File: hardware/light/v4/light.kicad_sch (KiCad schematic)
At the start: 18 parts, among them J1 PH2-16-UA, J2 Conn_01x09, J3 Conn_01x09, J4 B3B-XH-A, Q1 DMG2301L, Q2 MMBT3904, U1 LP2985-50DBVR, U2 SN74LVC1G17DBVR

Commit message: Wordsmithing and link to firmware repo.
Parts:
- added D1: 5.1V, Diode_SMD:D_SOD-123, symbol Device:D_Zener
- added R5: 100K, Resistor_SMD:R_0603_1608Metric, symbol Device:R
- Q1: value DMG2301L -> SI2301CDS; Alternative (none) -> DMG2301L; LCSC C102619 -> C10487; LCSC_Alternative (none) -> C102619
- renumbered R5 to R6, R6 to R7
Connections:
- net +12V: now also D1.1 (K)
- net GND: now also R5.1
- net LOAD: now also R5.2
- net at Q1.1 (G), R1.2, R2.2: now also D1.2 (A)
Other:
- note added: "Suitable for PWM switching LEDs at 1 KHz"
- note removed: "Suitable for PWM switching at low frequencies (< 1 KHz) DMG2301L parameters - Vgss max = -8 V - Vdss max = -20 V - Id max = -3 A - Rds(on) max = 120 mOhm"
- moved on the sheet: C1, C2, C3, J1, J2, J3, J4, JP1, Q1, R3, R4, R6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

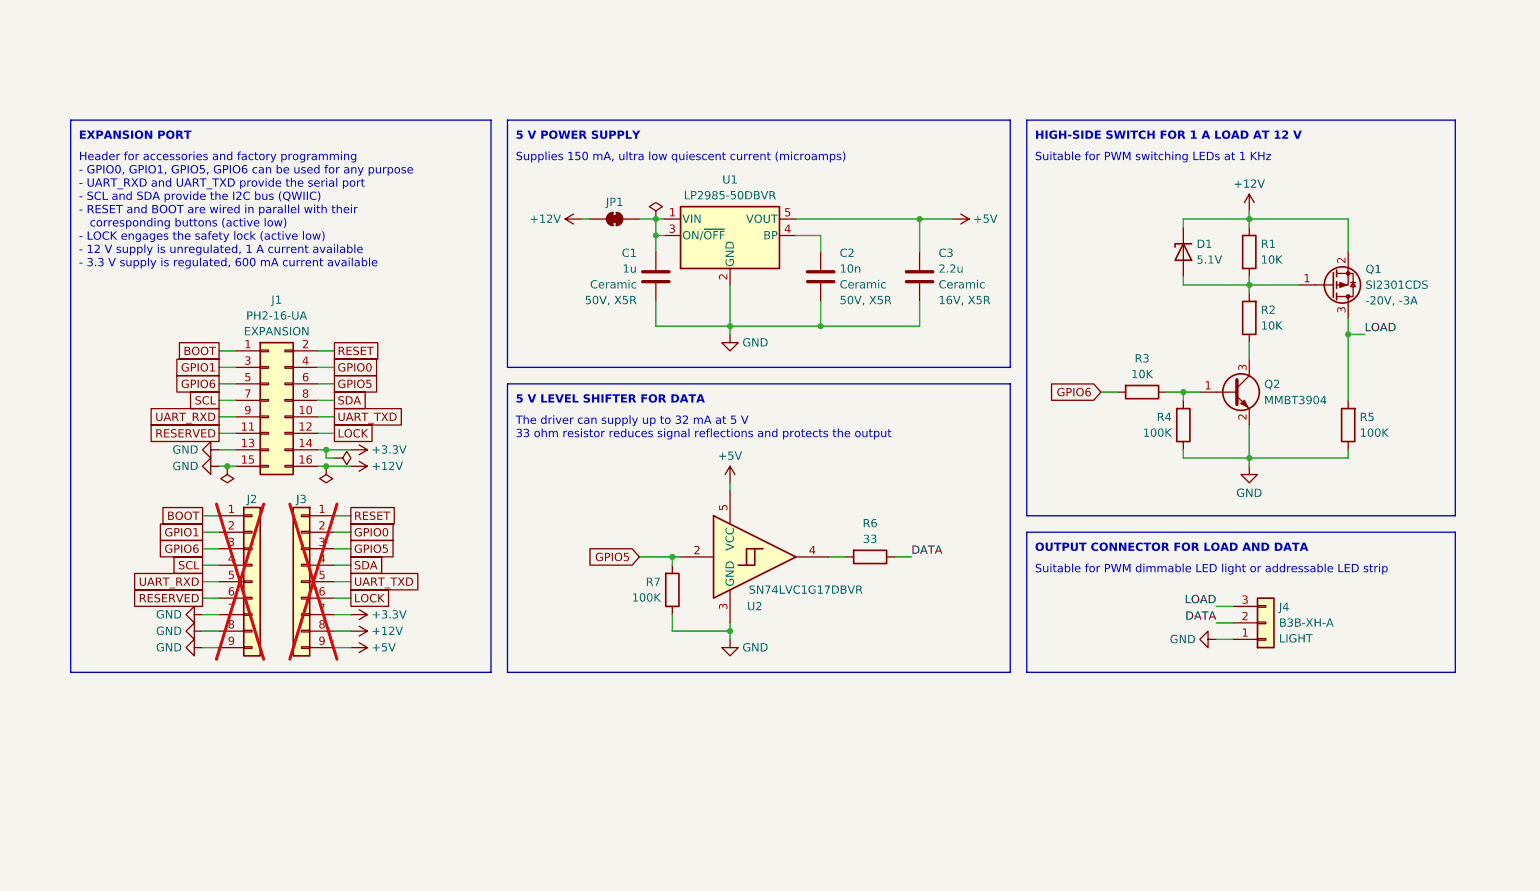
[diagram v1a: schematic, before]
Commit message: First draft of Minuet light accessory v4.
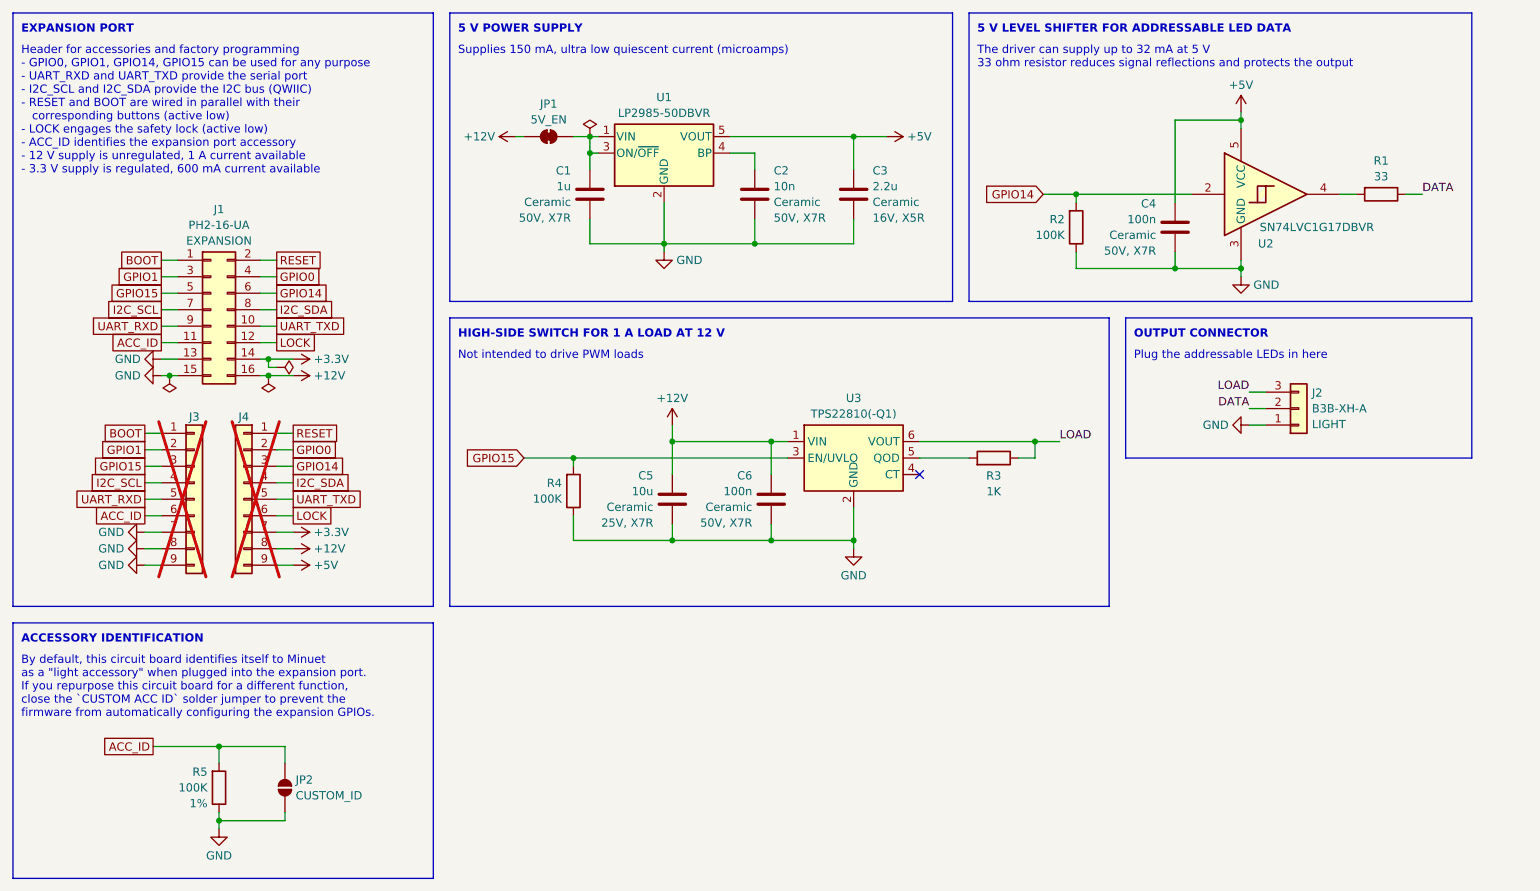
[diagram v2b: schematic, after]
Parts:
- removed D1: 5.1V, Diode_SMD:D_SOD-123, symbol Device:D_Zener
- removed Q1: SI2301CDS, Package_TO_SOT_SMD:SOT-23, symbol Transistor_FET:Q_PMOS_GSD
- removed Q2: MMBT3904, Package_TO_SOT_SMD:SOT-23, symbol Transistor_BJT:MMBT3904
- removed R1, R2: 10K, Resistor_SMD:R_0603_1608Metric, symbol Device:R
- added C4, C6: 100n, Capacitor_SMD:C_0603_1608Metric, symbol Device:C
- added C5: 10u, Capacitor_SMD:C_1210_3225Metric, symbol Device:C
- added JP2: SolderJumper_2_Open, Jumper:SolderJumper-2_P1.3mm_Open_RoundedPad1.0x1.5mm, symbol Jumper:SolderJumper_2_Open
- added U3: TPS22810(-Q1), Package_TO_SOT_SMD:SOT-23-6, symbol Power_Management:TPS22810DBV
- C1: footprint Capacitor_SMD:C_0603_1608Metric -> Capacitor_SMD:C_0805_2012Metric; LCSC C15849 -> C28323; Rating 50V, X5R -> 50V, X7R
- C2: Rating 50V, X5R -> 50V, X7R
- JP1: Label (none) -> 5V_EN
- R1: renamed from R6; Rating (none) -> 1%
- R2: renamed from R7; Rating (none) -> 1%
- R3: value 10K -> 1K; LCSC C25804 -> C21190; Rating (none) -> 1%
- R4, R5: Rating (none) -> 1%
- renumbered J4 to J2, J2 to J3, J3 to J4
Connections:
- net +12V: now also C5.1, C6.1, U3.1 (VIN)
- net +5V: now also C4.1
- net GND: now also C4.2, C5.2, C6.2, JP2.2 (B), U3.2 (GND)
- net LOAD: now also R3.1, U3.6 (VOUT); no longer R5.2
- net GPIO15: now reaches R4.2
- net GPIO15: now also J1.5 (Pin_5), J3.3 (Pin_3), U3.3 (EN/UVLO); no longer R3.1
- net GPIO5 renamed GPIO14
- removed net GPIO6: J1.5 (Pin_5), J3.3 (Pin_3), R3.2
- net RESERVED renamed ACC_ID
- net ACC_ID: now also R5.2, JP2.1 (A)
- net SCL renamed I2C_SCL
- net SDA renamed I2C_SDA
- new net: R3.2, U3.5 (QOD)
- no-connect marks 0 -> 1
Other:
- note added: "5 V LEVEL SHIFTER FOR ADDRESSABLE LED DATA"
- note added: "ACCESSORY IDENTIFICATION"
- note added: "By default, this circuit board identifies itself to Minuet as a "light accessory" when plugged into the expansion port. If you repurpose this circuit board for a different function, close the `CUSTOM ACC ID` solder jumper to prevent the firmware from automatically configuring the expansion GPIOs."
- note added: "Header for accessories and factory programming - GPIO0, GPIO1, GPIO14, GPIO15 can be used for any purpose - UART_RXD and UART_TXD provide the serial port - I2C_SCL and I2C_SDA provide the I2C bus (QWIIC) - RESET and BOOT are wired in parallel with their corresponding buttons (active low) - LOCK engages the safety lock (active low) - ACC_ID identifies the expansion port accessory - 12 V supply is 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"
- note added: "Not intended to drive PWM loads"
- note added: "OUTPUT CONNECTOR"
- note added: "Plug the addressable LEDs in here"
- note removed: "5 V LEVEL SHIFTER FOR DATA"
- note removed: "Header for accessories and factory programming - GPIO0, GPIO1, GPIO5, GPIO6 can be used for any purpose - UART_RXD and UART_TXD provide the serial port - SCL and SDA provide the I2C bus (QWIIC) - RESET and BOOT are wired in parallel with their corresponding buttons (active low) - LOCK engages the safety lock (active low) - 12 V supply is unregulated, 1 A current available - 3.3 V supply is regula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"
- note removed: "OUTPUT CONNECTOR FOR LOAD AND DATA"
- note removed: "Suitable for PWM dimmable LED light or addressable LED strip"
- note removed: "Suitable for PWM switching LEDs at 1 KHz"
- moved on the sheet: C1, C2, C3, J1, J2, J3, J4, JP1, R1, R2, U1, U2

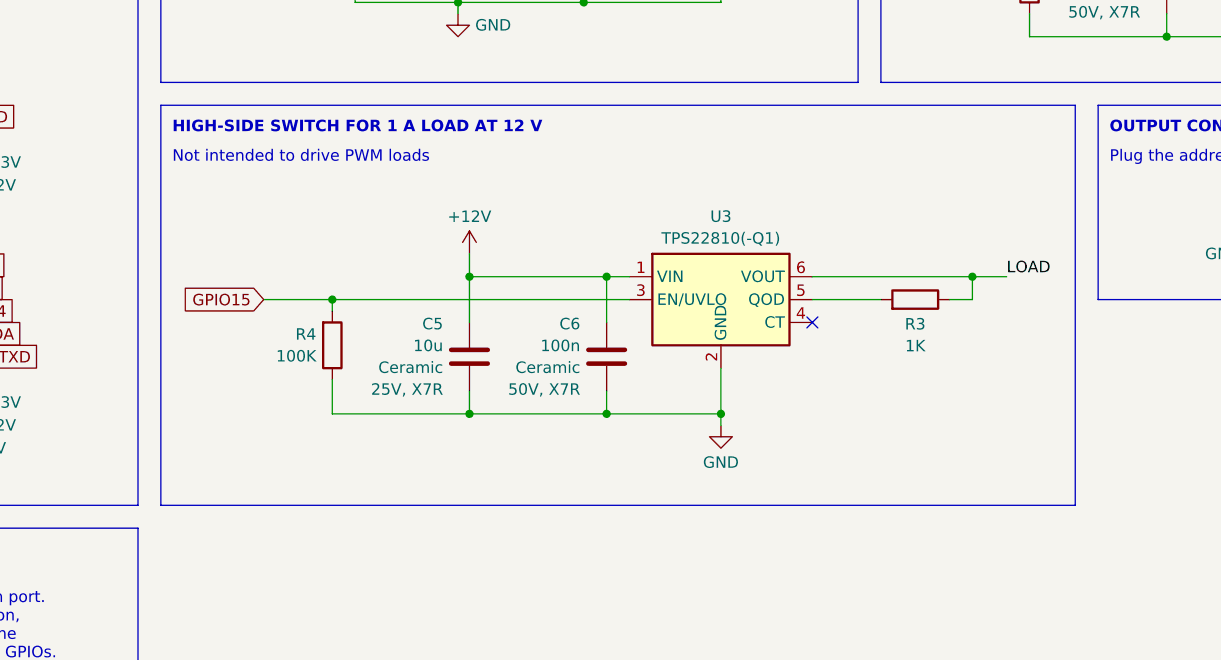
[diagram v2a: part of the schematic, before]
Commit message: Add DNP footprint for CT slew rate capacitor.
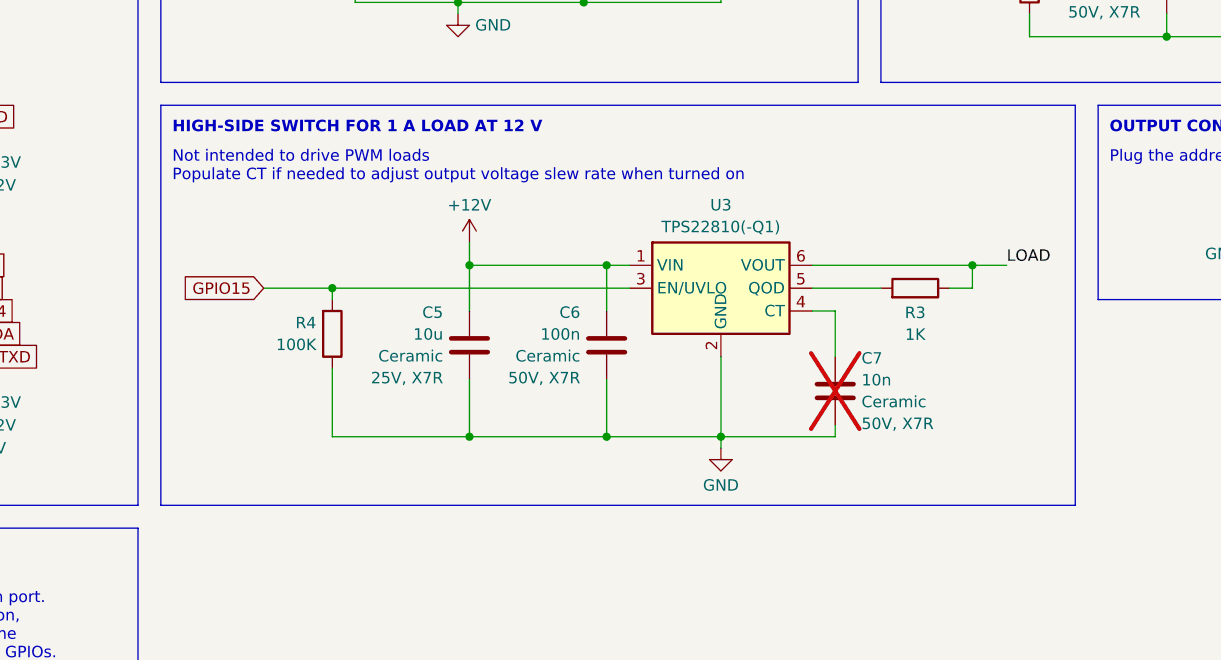
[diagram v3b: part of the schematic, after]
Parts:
- added C7: 10n, Capacitor_SMD:C_0603_1608Metric, symbol Device:C
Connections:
- net GND: now also C7.1
- net at U3.4 (CT): now also C7.2
- no-connect marks 1 -> 0
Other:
- note added: "Not intended to drive PWM loads Populate CT if needed to adjust output voltage slew rate when turned on"
- note removed: "Not intended to drive PWM loads"
- moved on the sheet: C5, C6, R3, R4, U3
